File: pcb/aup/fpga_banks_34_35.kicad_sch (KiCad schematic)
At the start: 1 part, among them U1 XC7A50T-2FGG484C

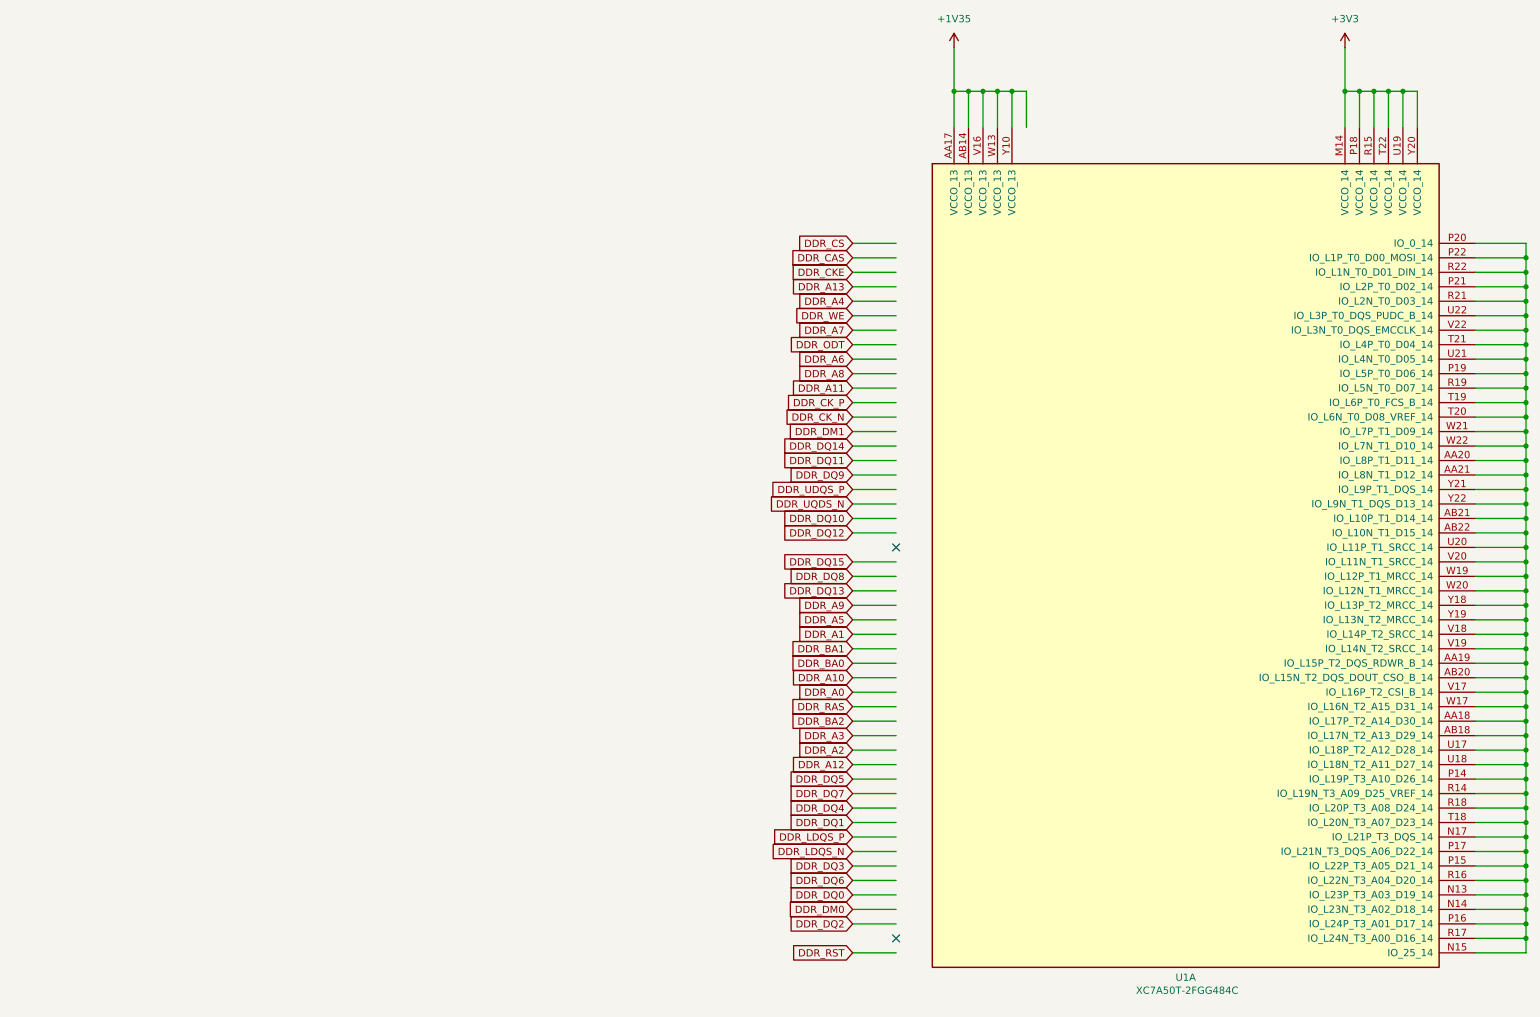
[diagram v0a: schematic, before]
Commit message: Add hierarchical sheets for banks and add caps.
There are some stale sheets in this commit, but I don't want to delete
an active one accidentally. Save them all for now, and then go back and
clean them up.
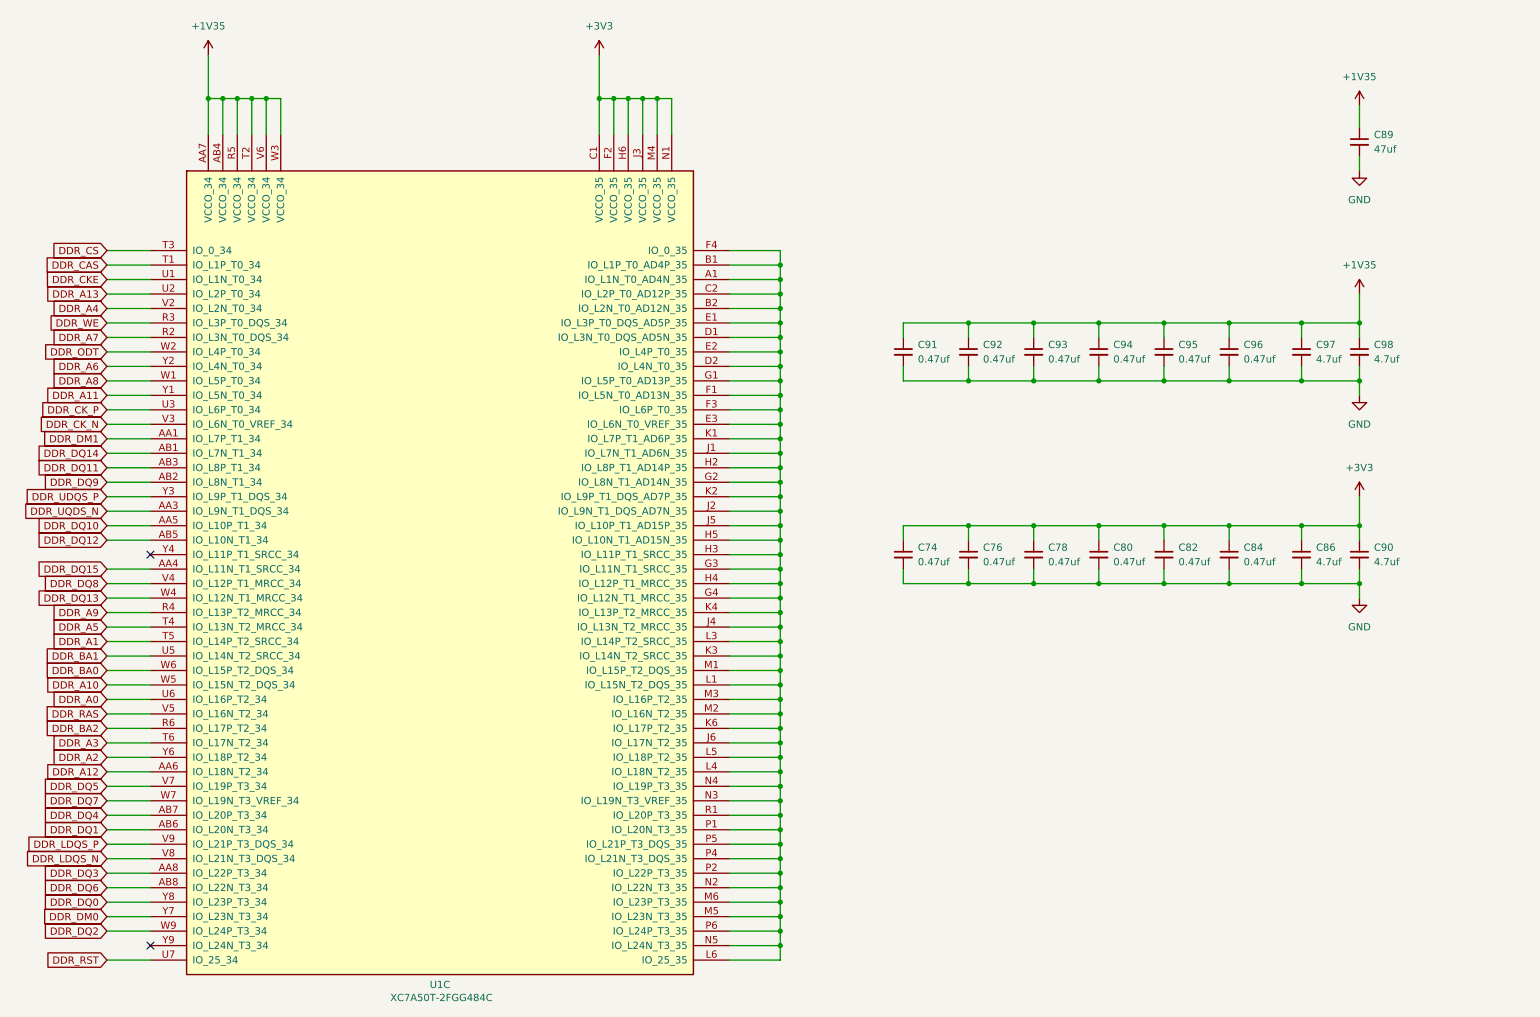
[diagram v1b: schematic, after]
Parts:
- added C74, C76, C78, C80, C82, C84, C91, C92, C93, C94, C95, C96: 0.47uf, Capacitor_SMD:C_0402_1005Metric, symbol !Misc:C_0.47uf_0402
- added C86, C90, C97, C98: 4.7uf, Capacitor_SMD:C_0805_2012Metric, symbol !Misc:C_4.7uf_0805
- added C89: 47uf, Capacitor_SMD:C_1206_3216Metric, symbol !Misc:C_47uf_1206
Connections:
- net +1V35: now also U1.AA7 (VCCO_34), U1.AB4 (VCCO_34), U1.R5 (VCCO_34), U1.T2 (VCCO_34), U1.V6 (VCCO_34), U1.W3 (VCCO_34), C89.1, C91.1, C92.1, C93.1, C94.1, C95.1, C96.1, C97.1, C98.1; no longer U1.AA17 (VCCO_13), U1.AB14 (VCCO_13), U1.V16 (VCCO_13), U1.W13 (VCCO_13), U1.Y10 (VCCO_13)
- net +3V3: now also U1.C1 (VCCO_35), U1.F2 (VCCO_35), U1.H6 (VCCO_35), U1.J3 (VCCO_35), U1.M4 (VCCO_35), U1.N1 (VCCO_35), C74.1, C76.1, C78.1, C80.1, C82.1, C84.1, C86.1, C90.1; no longer U1.M14 (VCCO_14), U1.P18 (VCCO_14), U1.R15 (VCCO_14), U1.T22 (VCCO_14), U1.U19 (VCCO_14), U1.Y20 (VCCO_14)
- net DDR_A0: now also U1.U6 (IO_L16P_T2_34)
- net DDR_A1: now also U1.T5 (IO_L14P_T2_SRCC_34)
- net DDR_A10: now also U1.W5 (IO_L15N_T2_DQS_34)
- net DDR_A11: now also U1.Y1 (IO_L5N_T0_34)
- net DDR_A12: now also U1.AA6 (IO_L18N_T2_34)
- net DDR_A13: now also U1.U2 (IO_L2P_T0_34)
- net DDR_A2: now also U1.Y6 (IO_L18P_T2_34)
- net DDR_A3: now also U1.T6 (IO_L17N_T2_34)
- net DDR_A4: now also U1.V2 (IO_L2N_T0_34)
- net DDR_A5: now also U1.T4 (IO_L13N_T2_MRCC_34)
- net DDR_A6: now also U1.Y2 (IO_L4N_T0_34)
- net DDR_A7: now also U1.R2 (IO_L3N_T0_DQS_34)
- net DDR_A8: now also U1.W1 (IO_L5P_T0_34)
- net DDR_A9: now also U1.R4 (IO_L13P_T2_MRCC_34)
- net DDR_BA0: now also U1.W6 (IO_L15P_T2_DQS_34)
- net DDR_BA1: now also U1.U5 (IO_L14N_T2_SRCC_34)
- net DDR_BA2: now also U1.R6 (IO_L17P_T2_34)
- net DDR_CAS: now also U1.T1 (IO_L1P_T0_34)
- net DDR_CKE: now also U1.U1 (IO_L1N_T0_34)
- net DDR_CK_N: now also U1.V3 (IO_L6N_T0_VREF_34)
- net DDR_CK_P: now also U1.U3 (IO_L6P_T0_34)
- net DDR_CS: now also U1.T3 (IO_0_34)
- net DDR_DM0: now also U1.Y7 (IO_L23N_T3_34)
- net DDR_DM1: now also U1.AA1 (IO_L7P_T1_34)
- net DDR_DQ0: now also U1.Y8 (IO_L23P_T3_34)
- net DDR_DQ1: now also U1.AB6 (IO_L20N_T3_34)
- net DDR_DQ10: now also U1.AA5 (IO_L10P_T1_34)
- net DDR_DQ11: now also U1.AB3 (IO_L8P_T1_34)
- net DDR_DQ12: now also U1.AB5 (IO_L10N_T1_34)
- net DDR_DQ13: now also U1.W4 (IO_L12N_T1_MRCC_34)
- net DDR_DQ14: now also U1.AB1 (IO_L7N_T1_34)
- net DDR_DQ15: now also U1.AA4 (IO_L11N_T1_SRCC_34)
- net DDR_DQ2: now also U1.W9 (IO_L24P_T3_34)
- net DDR_DQ3: now also U1.AA8 (IO_L22P_T3_34)
- net DDR_DQ4: now also U1.AB7 (IO_L20P_T3_34)
- net DDR_DQ5: now also U1.V7 (IO_L19P_T3_34)
- net DDR_DQ6: now also U1.AB8 (IO_L22N_T3_34)
- net DDR_DQ7: now also U1.W7 (IO_L19N_T3_VREF_34)
- net DDR_DQ8: now also U1.V4 (IO_L12P_T1_MRCC_34)
- net DDR_DQ9: now also U1.AB2 (IO_L8N_T1_34)
- net DDR_LDQS_N: now also U1.V8 (IO_L21N_T3_DQS_34)
- net DDR_LDQS_P: now also U1.V9 (IO_L21P_T3_DQS_34)
- net DDR_ODT: now also U1.W2 (IO_L4P_T0_34)
- net DDR_RAS: now also U1.V5 (IO_L16N_T2_34)
- net DDR_RST: now also U1.U7 (IO_25_34)
- net DDR_UDQS_P: now also U1.Y3 (IO_L9P_T1_DQS_34)
- net DDR_UQDS_N: now also U1.AA3 (IO_L9N_T1_DQS_34)
- net DDR_WE: now also U1.R3 (IO_L3P_T0_DQS_34)
- new net: U1.A1 (IO_L1N_T0_AD4N_35), U1.B1 (IO_L1P_T0_AD4P_35), U1.B2 (IO_L2N_T0_AD12N_35), U1.C2 (IO_L2P_T0_AD12P_35), U1.D1 (IO_L3N_T0_DQS_AD5N_35), U1.D2 (IO_L4N_T0_35), U1.E1 (IO_L3P_T0_DQS_AD5P_35), U1.E2 (IO_L4P_T0_35), U1.E3 (IO_L6N_T0_VREF_35), U1.F1 (IO_L5N_T0_AD13N_35), U1.F3 (IO_L6P_T0_35), U1.F4 (IO_0_35), U1.G1 (IO_L5P_T0_AD13P_35), U1.G2 (IO_L8N_T1_AD14N_35), U1.G3 (IO_L11N_T1_SRCC_35), U1.G4 (IO_L12N_T1_MRCC_35), U1.H2 (IO_L8P_T1_AD14P_35), U1.H3 (IO_L11P_T1_SRCC_35), U1.H4 (IO_L12P_T1_MRCC_35), U1.H5 (IO_L10N_T1_AD15N_35), U1.J1 (IO_L7N_T1_AD6N_35), U1.J2 (IO_L9N_T1_DQS_AD7N_35), U1.J4 (IO_L13N_T2_MRCC_35), U1.J5 (IO_L10P_T1_AD15P_35), U1.J6 (IO_L17N_T2_35), U1.K1 (IO_L7P_T1_AD6P_35), U1.K2 (IO_L9P_T1_DQS_AD7P_35), U1.K3 (IO_L14N_T2_SRCC_35), U1.K4 (IO_L13P_T2_MRCC_35), U1.K6 (IO_L17P_T2_35), U1.L1 (IO_L15N_T2_DQS_35), U1.L3 (IO_L14P_T2_SRCC_35), U1.L4 (IO_L18N_T2_35), U1.L5 (IO_L18P_T2_35), U1.L6 (IO_25_35), U1.M1 (IO_L15P_T2_DQS_35), U1.M2 (IO_L16N_T2_35), U1.M3 (IO_L16P_T2_35), U1.M5 (IO_L23N_T3_35), U1.M6 (IO_L23P_T3_35), U1.N2 (IO_L22N_T3_35), U1.N3 (IO_L19N_T3_VREF_35), U1.N4 (IO_L19P_T3_35), U1.N5 (IO_L24N_T3_35), U1.P1 (IO_L20N_T3_35), U1.P2 (IO_L22P_T3_35), U1.P4 (IO_L21N_T3_DQS_35), U1.P5 (IO_L21P_T3_DQS_35), U1.P6 (IO_L24P_T3_35), U1.R1 (IO_L20P_T3_35)
- new net GND: C74.2, C76.2, C78.2, C80.2, C82.2, C84.2, C86.2, C89.2, C90.2, C91.2, C92.2, C93.2, C94.2, C95.2, C96.2, C97.2, C98.2

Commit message: Switch 0.47uf caps under bga to 0201
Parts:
- C74, C76, C78, C80, C82, C84, C91, C92, C93, C94, C95, C96: footprint Capacitor_SMD:C_0402_1005Metric -> Capacitor_SMD:C_0201_0603Metric; symbol !Misc:C_0.47uf_0402 -> !Misc:C_0.47uf_0201; Digi-Key Part Number 1276-1173-1-ND -> 1276-1337-1-ND; LCSC Part # C1779 -> C318543
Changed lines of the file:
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@@
 	)
 	(symbol
-		(lib_id "!Misc:C_0.47uf_0402")
+		(lib_id "!Misc:C_0.47uf_0201")
 		(at 215.9 111.76 0)
 		(unit 1)
@@
 			)
 		)
-		(property "Footprint" "Capacitor_SMD:C_0402_1005Metric"
+		(property "Footprint" "Capacitor_SMD:C_0201_0603Metric"
 			(at 215.9 111.76 0)
 			(effects
@@
 			)
 		)
-		(property "Description" "Unpolarized capacitor 0.47uf 0402"
+		(property "Description" "Unpolarized capacitor 0.47uf 0201"
 			(at 215.9 111.76 0)
 			(effects
@@
 			)
 		)
-		(property "LCSC Part #" "C1779"
+		(property "LCSC Part #" "C318543"
 			(at 215.9 111.76 0)
 			(effects
@@
 			)
 		)
-		(property "Digi-Key Part Number" "1276-1173-1-ND"
+		(property "Digi-Key Part Number" "1276-1337-1-ND"
 			(at 215.9 111.76 0)
 			(effects
@@
 	)
 	(symbol
-		(lib_id "!Misc:C_0.47uf_0402")
+		(lib_id "!Misc:C_0.47uf_0201")
 		(at 250.19 76.2 0)
 		(unit 1)
@@
 			)
 		)
-		(property "Footprint" "Capacitor_SMD:C_0402_1005Metric"
+		(property "Footprint" "Capacitor_SMD:C_0201_0603Metric"
 			(at 250.19 76.2 0)
 			(effects
@@
 			)
 		)
-		(property "Description" "Unpolarized capacitor 0.47uf 0402"
+		(property "Description" "Unpolarized capacitor 0.47uf 0201"
 			(at 250.19 76.2 0)
 			(effects
@@
 			)
 		)
-		(property "LCSC Part #" "C1779"
+		(property "LCSC Part #" "C318543"
 			(at 250.19 76.2 0)
 			(effects
@@
 			)
 		)
-		(property "Digi-Key Part Number" "1276-1173-1-ND"
+		(property "Digi-Key Part Number" "1276-1337-1-ND"
 			(at 250.19 76.2 0)
 			(effects
@@
 	)
 	(symbol
-		(lib_id "!Misc:C_0.47uf_0402")
+		(lib_id "!Misc:C_0.47uf_0201")
 		(at 238.76 76.2 0)
 		(unit 1)
@@
 			)
 		)
-		(property "Footprint" "Capacitor_SMD:C_0402_1005Metric"
+		(property "Footprint" "Capacitor_SMD:C_0201_0603Metric"
 			(at 238.76 76.2 0)
 			(effects
@@
 			)
 		)
-		(property "Description" "Unpolarized capacitor 0.47uf 0402"
+		(property "Description" "Unpolarized capacitor 0.47uf 0201"
 			(at 238.76 76.2 0)
 			(effects
@@
 			)
 		)
-		(property "LCSC Part #" "C1779"
+		(property "LCSC Part #" "C318543"
 			(at 238.76 76.2 0)
 			(effects
@@
 			)
 		)
-		(property "Digi-Key Part Number" "1276-1173-1-ND"
+		(property "Digi-Key Part Number" "1276-1337-1-ND"
 			(at 238.76 76.2 0)
 			(effects
@@
 	)
 	(symbol
-		(lib_id "!Misc:C_0.47uf_0402")
+		(lib_id "!Misc:C_0.47uf_0201")
 		(at 193.04 111.76 0)
 		(unit 1)
@@
 			)
 		)
-		(property "Footprint" "Capacitor_SMD:C_0402_1005Metric"
+		(property "Footprint" "Capacitor_SMD:C_0201_0603Metric"
 			(at 193.04 111.76 0)
 			(effects
@@
 			)
 		)
-		(property "Description" "Unpolarized capacitor 0.47uf 0402"
+		(property "Description" "Unpolarized capacitor 0.47uf 0201"
 			(at 193.04 111.76 0)
 			(effects
@@
 			)
 		)
-		(property "LCSC Part #" "C1779"
+		(property "LCSC Part #" "C318543"
 			(at 193.04 111.76 0)
 			(effects
@@
 			)
 		)
-		(property "Digi-Key Part Number" "1276-1173-1-ND"
+		(property "Digi-Key Part Number" "1276-1337-1-ND"
 			(at 193.04 111.76 0)
 			(effects
@@
 	)
 	(symbol
-		(lib_id "!Misc:C_0.47uf_0402")
+		(lib_id "!Misc:C_0.47uf_0201")
 		(at 193.04 76.2 0)
 		(unit 1)
@@
 			)
 		)
-		(property "Footprint" "Capacitor_SMD:C_0402_1005Metric"
+		(property "Footprint" "Capacitor_SMD:C_0201_0603Metric"
 			(at 193.04 76.2 0)
 			(effects
@@
 			)
 		)
-		(property "Description" "Unpolarized capacitor 0.47uf 0402"
+		(property "Description" "Unpolarized capacitor 0.47uf 0201"
 			(at 193.04 76.2 0)
 			(effects
@@
 			)
 		)
-		(property "LCSC Part #" "C1779"
+		(property "LCSC Part #" "C318543"
 			(at 193.04 76.2 0)
 			(effects
@@
 			)
 		)
-		(property "Digi-Key Part Number" "1276-1173-1-ND"
+		(property "Digi-Key Part Number" "1276-1337-1-ND"
 			(at 193.04 76.2 0)
 			(effects
@@
 	)
 	(symbol
-		(lib_id "!Misc:C_0.47uf_0402")
+		(lib_id "!Misc:C_0.47uf_0201")
 		(at 204.47 111.76 0)
 		(unit 1)
@@
 			)
 		)
-		(property "Footprint" "Capacitor_SMD:C_0402_1005Metric"
+		(property "Footprint" "Capacitor_SMD:C_0201_0603Metric"
 			(at 204.47 111.76 0)
 			(effects
@@
 			)
 		)
-		(property "Description" "Unpolarized capacitor 0.47uf 0402"
+		(property "Description" "Unpolarized capacitor 0.47uf 0201"
 			(at 204.47 111.76 0)
 			(effects
@@
 			)
 		)
-		(property "LCSC Part #" "C1779"
+		(property "LCSC Part #" "C318543"
 			(at 204.47 111.76 0)
 			(effects
@@
 			)
 		)
-		(property "Digi-Key Part Number" "1276-1173-1-ND"
+		(property "Digi-Key Part Number" "1276-1337-1-ND"
 			(at 204.47 111.76 0)
 			(effects
@@
 	)
 	(symbol
-		(lib_id "!Misc:C_0.47uf_0402")
+		(lib_id "!Misc:C_0.47uf_0201")
 		(at 238.76 111.76 0)
 		(unit 1)
@@
 			)
 		)
-		(property "Footprint" "Capacitor_SMD:C_0402_1005Metric"
+		(property "Footprint" "Capacitor_SMD:C_0201_0603Metric"
 			(at 238.76 111.76 0)
 			(effects
@@
 			)
 		)
-		(property "Description" "Unpolarized capacitor 0.47uf 0402"
+		(property "Description" "Unpolarized capacitor 0.47uf 0201"
 			(at 238.76 111.76 0)
 			(effects
@@
 			)
 		)
-		(property "LCSC Part #" "C1779"
+		(property "LCSC Part #" "C318543"
 			(at 238.76 111.76 0)
 			(effects
@@
 			)
 		)
-		(property "Digi-Key Part Number" "1276-1173-1-ND"
+		(property "Digi-Key Part Number" "1276-1337-1-ND"
 			(at 238.76 111.76 0)
 			(effects
@@
 	)
 	(symbol
-		(lib_id "!Misc:C_0.47uf_0402")
+		(lib_id "!Misc:C_0.47uf_0201")
 		(at 250.19 111.76 0)
 		(unit 1)
@@
 			)
 		)
-		(property "Footprint" "Capacitor_SMD:C_0402_1005Metric"
+		(property "Footprint" "Capacitor_SMD:C_0201_0603Metric"
 			(at 250.19 111.76 0)
 			(effects
@@
 			)
 		)
-		(property "Description" "Unpolarized capacitor 0.47uf 0402"
+		(property "Description" "Unpolarized capacitor 0.47uf 0201"
 			(at 250.19 111.76 0)
 			(effects
@@
 			)
 		)
-		(property "LCSC Part #" "C1779"
+		(property "LCSC Part #" "C318543"
 			(at 250.19 111.76 0)
 			(effects
@@
 			)
 		)
-		(property "Digi-Key Part Number" "1276-1173-1-ND"
+		(property "Digi-Key Part Number" "1276-1337-1-ND"
 			(at 250.19 111.76 0)
 			(effects
@@
 	)
 	(symbol
-		(lib_id "!Misc:C_0.47uf_0402")
+		(lib_id "!Misc:C_0.47uf_0201")
 		(at 204.47 76.2 0)
 		(unit 1)
@@
 			)
 		)
-		(property "Footprint" "Capacitor_SMD:C_0402_1005Metric"
+		(property "Footprint" "Capacitor_SMD:C_0201_0603Metric"
 			(at 204.47 76.2 0)
 			(effects
@@
 			)
 		)
-		(property "Description" "Unpolarized capacitor 0.47uf 0402"
+		(property "Description" "Unpolarized capacitor 0.47uf 0201"
 			(at 204.47 76.2 0)
 			(effects
@@
 			)
 		)
-		(property "LCSC Part #" "C1779"
+		(property "LCSC Part #" "C318543"
 			(at 204.47 76.2 0)
 			(effects
@@
 			)
 		)
-		(property "Digi-Key Part Number" "1276-1173-1-ND"
+		(property "Digi-Key Part Number" "1276-1337-1-ND"
 			(at 204.47 76.2 0)
 			(effects
@@
 	)
 	(symbol
-		(lib_id "!Misc:C_0.47uf_0402")
+		(lib_id "!Misc:C_0.47uf_0201")
 		(at 227.33 76.2 0)
 		(unit 1)
@@
 			)
 		)
-		(property "Footprint" "Capacitor_SMD:C_0402_1005Metric"
+		(property "Footprint" "Capacitor_SMD:C_0201_0603Metric"
 			(at 227.33 76.2 0)
 			(effects
@@
 			)
 		)
-		(property "Description" "Unpolarized capacitor 0.47uf 0402"
+		(property "Description" "Unpolarized capacitor 0.47uf 0201"
 			(at 227.33 76.2 0)
 			(effects
@@
 			)
 		)
-		(property "LCSC Part #" "C1779"
+		(property "LCSC Part #" "C318543"
 			(at 227.33 76.2 0)
 			(effects
@@
 			)
 		)
-		(property "Digi-Key Part Number" "1276-1173-1-ND"
+		(property "Digi-Key Part Number" "1276-1337-1-ND"
 			(at 227.33 76.2 0)
 			(effects
@@
 	)
 	(symbol
-		(lib_id "!Misc:C_0.47uf_0402")
+		(lib_id "!Misc:C_0.47uf_0201")
 		(at 227.33 111.76 0)
 		(unit 1)
@@
 			)
 		)
-		(property "Footprint" "Capacitor_SMD:C_0402_1005Metric"
+		(property "Footprint" "Capacitor_SMD:C_0201_0603Metric"
 			(at 227.33 111.76 0)
 			(effects
@@
 			)
 		)
-		(property "Description" "Unpolarized capacitor 0.47uf 0402"
+		(property "Description" "Unpolarized capacitor 0.47uf 0201"
 			(at 227.33 111.76 0)
 			(effects
@@
 			)
 		)
-		(property "LCSC Part #" "C1779"
+		(property "LCSC Part #" "C318543"
 			(at 227.33 111.76 0)
 			(effects
@@
 			)
 		)
-		(property "Digi-Key Part Number" "1276-1173-1-ND"
+		(property "Digi-Key Part Number" "1276-1337-1-ND"
 			(at 227.33 111.76 0)
 			(effects
@@
 	)
 	(symbol
-		(lib_id "!Misc:C_0.47uf_0402")
+		(lib_id "!Misc:C_0.47uf_0201")
 		(at 215.9 76.2 0)
 		(unit 1)
@@
 			)
 		)
-		(property "Footprint" "Capacitor_SMD:C_0402_1005Metric"
+		(property "Footprint" "Capacitor_SMD:C_0201_0603Metric"
 			(at 215.9 76.2 0)
 			(effects
@@
 			)
 		)
-		(property "Description" "Unpolarized capacitor 0.47uf 0402"
+		(property "Description" "Unpolarized capacitor 0.47uf 0201"
 			(at 215.9 76.2 0)
 			(effects
@@
 			)
 		)
-		(property "LCSC Part #" "C1779"
+		(property "LCSC Part #" "C318543"
 			(at 215.9 76.2 0)
 			(effects
@@
 			)
 		)
-		(property "Digi-Key Part Number" "1276-1173-1-ND"
+		(property "Digi-Key Part Number" "1276-1337-1-ND"
 			(at 215.9 76.2 0)
 			(effects
